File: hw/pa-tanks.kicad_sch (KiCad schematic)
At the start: 62 parts, among them K2202 G2RL-1A, K2203 G2RL-1A, K2204 G2RL-1A, Q2201 2N7002, Q2202 2N7002, Q2203 2N7002, Q2204 2N7002, Q2205 2N7002, Q2206 2N7002, Q2207 2N7002, Q2208 2N7002, Q2209 2N7002, Q2210 2N7002

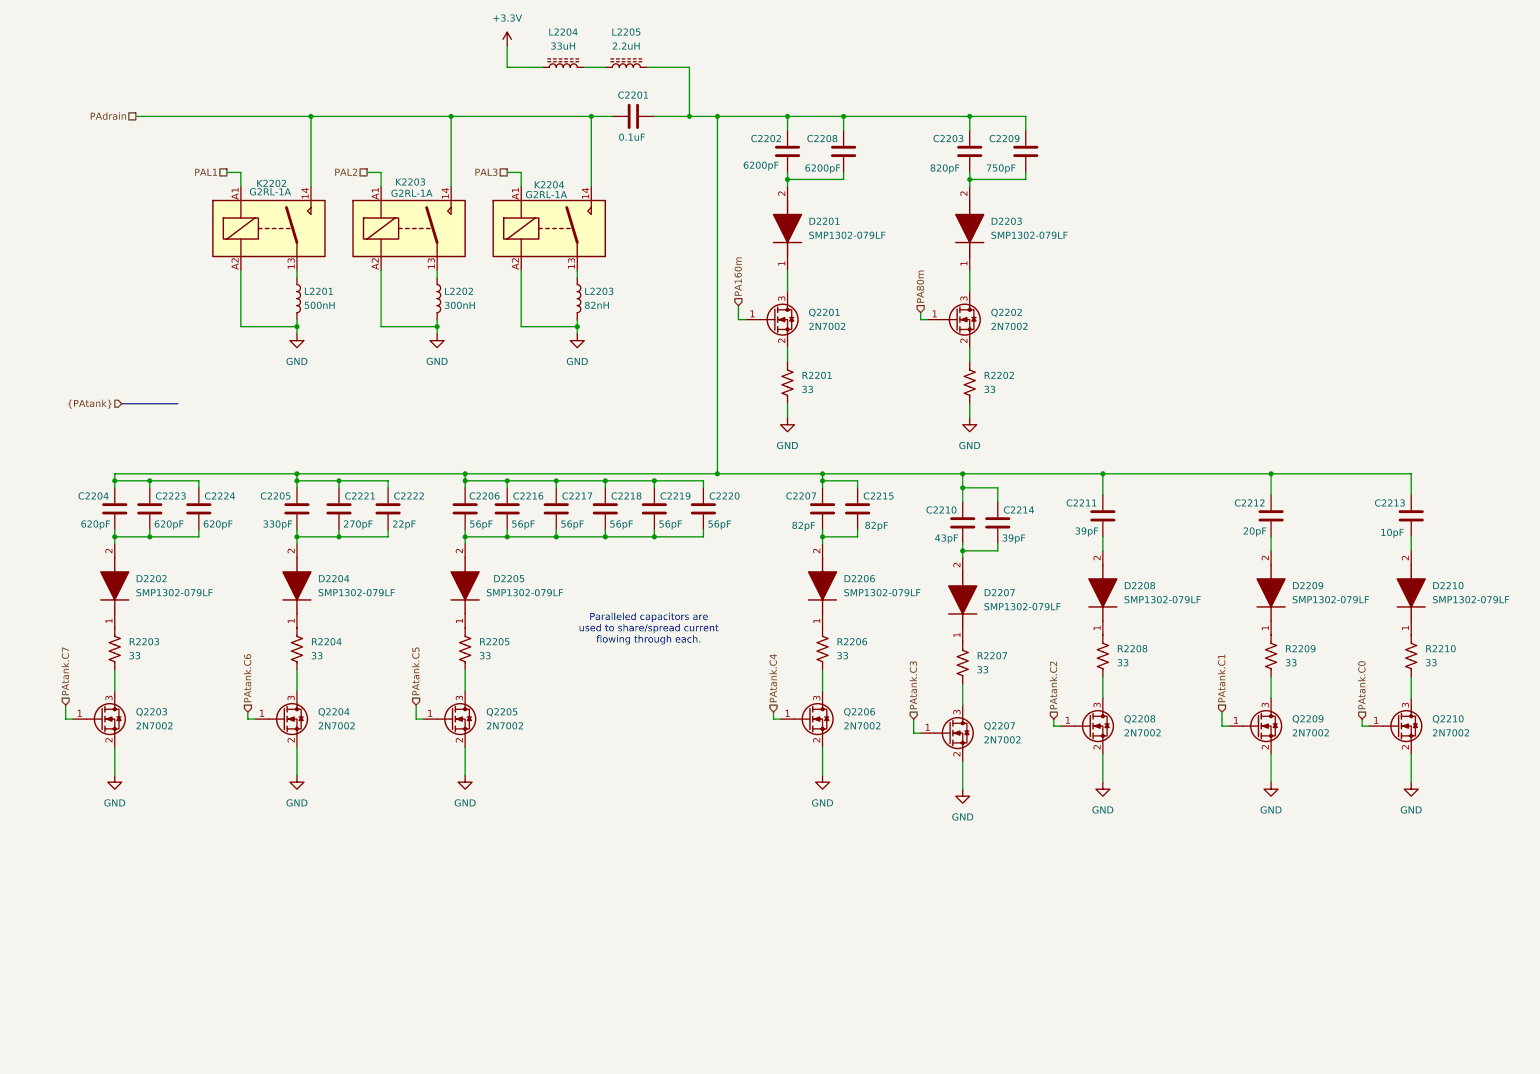
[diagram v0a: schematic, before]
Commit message: Getting closer to having the PA LC tank switching done
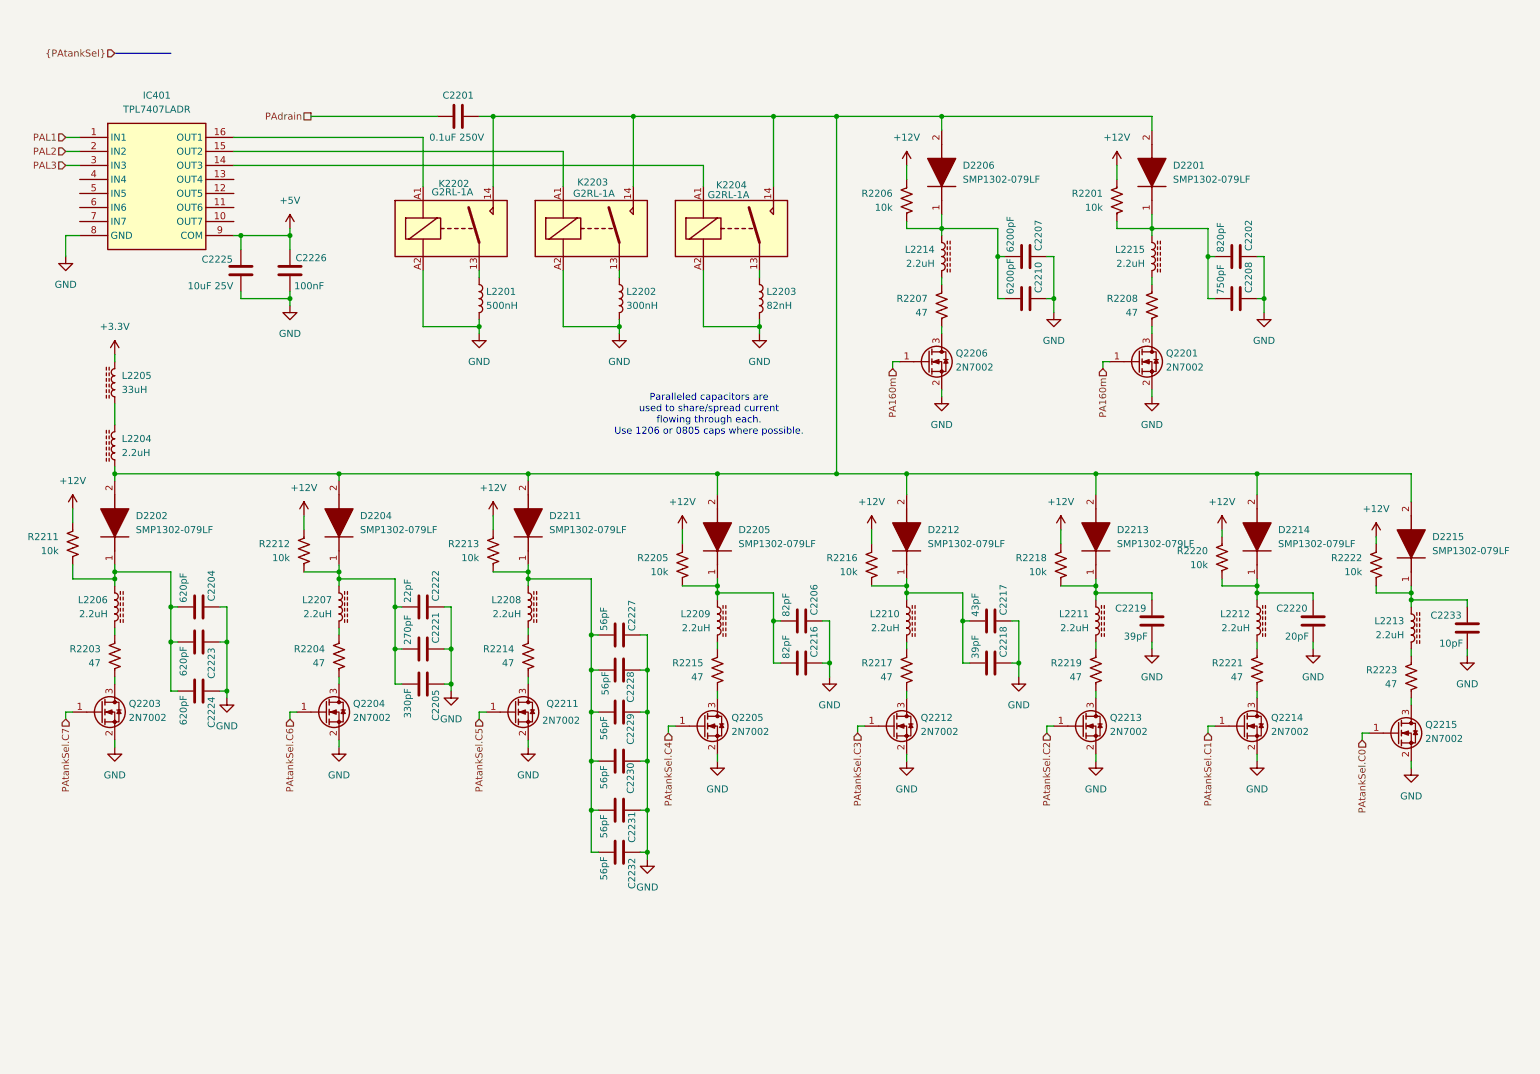
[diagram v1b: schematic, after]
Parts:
- removed C2203: 820pF, symbol Device:C
- removed C2209: 750pF, symbol Device:C
- removed C2211, C2214: 39pF, symbol Device:C
- removed C2212: 20pF, symbol Device:C
- removed C2213: 10pF, symbol Device:C
- removed C2215: 82pF, symbol Device:C
- removed D2203, D2207, D2208, D2209, D2210: SMP1302-079LF, SODFL1608X70N, symbol SMP1302-079LF:SMP1302-079LF
- removed Q2202, Q2207, Q2208, Q2209, Q2210: 2N7002, Package_TO_SOT_SMD:SOT-23, symbol Transistor_FET:2N7002
- removed R2202, R2209, R2210: 33, symbol Device:R_US
- added C2225: 10uF 25V, symbol Device:C
- added C2226: 100nF, symbol Device:C
- added C2227, C2228, C2229, C2230, C2231, C2232: 56pF, symbol Device:C
- added C2233: 10pF, symbol Device:C
- added D2211, D2212, D2213, D2214, D2215: SMP1302-079LF, SODFL1608X70N, symbol SMP1302-079LF:SMP1302-079LF
- added IC401: TPL7407LADR, SOIC127P600X175-16N, symbol TPL7407LADR:TPL7407LADR
- added L2206, L2207, L2208, L2209, L2210, L2211, L2212, L2213, L2214, L2215: 2.2uH, symbol Device:L_Ferrite
- added Q2211, Q2212, Q2213, Q2214, Q2215: 2N7002, Package_TO_SOT_SMD:SOT-23, symbol Transistor_FET:2N7002
- added R2211, R2212, R2213, R2216, R2218, R2220, R2222: 10k, symbol Device:R_US
- added R2214, R2215, R2217, R2219, R2221, R2223: 47, symbol Device:R_US
- C2201: value 0.1uF -> 0.1uF 250V
- C2202: value 6200pF -> 820pF
- C2206, C2216: value 56pF -> 82pF
- C2207: value 82pF -> 6200pF
- C2208: value 6200pF -> 750pF
- C2210: value 43pF -> 6200pF
- C2217: value 56pF -> 43pF
- C2218, C2219: value 56pF -> 39pF
- C2220: value 56pF -> 20pF
- L2204: value 33uH -> 2.2uH
- L2205: value 2.2uH -> 33uH
- R2201, R2205, R2206: value 33 -> 10k
- R2203, R2204, R2207, R2208: value 33 -> 47
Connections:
- net PAtank.C4 is gone; now on net PA160m: Q2206.1 (G)
- net +3.3V: now also L2205.2; no longer L2204.1
- net GND: now also C2202.2, C2204.2, C2205.2, C2206.2, C2207.2, C2208.2, C2210.2, C2216.2, C2217.2, C2218.2, C2219.1, C2220.1, C2221.2, C2222.2, C2223.2, C2224.2, Q2201.2 (S), C2225.1, C2226.1, C2227.2, C2228.2, C2229.2, C2230.2, C2231.2, C2232.2, C2233.1, IC401.8 (GND), Q2211.2 (S), Q2212.2 (S), Q2213.2 (S), Q2214.2 (S), Q2215.2 (S); no longer R2201.2
- net PAL1: now also IC401.1 (IN1); no longer K2202.A1
- net PAL2: now also IC401.2 (IN2); no longer K2203.A1
- net PAL3: now also IC401.3 (IN3); no longer K2204.A1
- net PAdrain: no longer K2202.14, K2203.14, K2204.14
- net at D2205.1 (K): now also C2206.1, C2216.1, R2205.2, L2209.2; no longer R2205.1
- net at R2208.2: now also Q2201.3 (D)
- net at D2206.2 (A): now also C2201.2, D2201.2 (A), D2202.2 (A), D2204.2 (A), D2205.2 (A), K2202.14, K2203.14, K2204.14, L2204.1, D2211.2 (A), D2212.2 (A), D2213.2 (A), D2214.2 (A), D2215.2 (A); no longer C2207.1
- net at C2210.1: now also C2207.1, D2206.1 (K), R2206.2, L2214.2
- net at Q2205.3 (D): now also R2215.2; no longer R2205.2
- net at C2204.1, C2223.1, C2224.1: now also D2202.1 (K), L2206.2, R2211.2; no longer D2202.2 (A)
- net at C2202.1, C2208.1: now also D2201.1 (K), R2201.2, L2215.2; no longer D2201.2 (A)
- net at R2207.1: now also L2214.1
- net +12V: now reaches R2206.1
- net +12V: now also R2201.1, R2205.1, R2211.1, R2212.1, R2213.1, R2216.1, R2218.1, R2220.1, R2222.1; no longer D2206.1 (K)
- net at Q2206.3 (D): now also R2207.2; no longer R2206.2
- net at R2203.1: now also L2206.1; no longer D2202.1 (K)
- net at C2205.1, C2221.1, C2222.1: now also D2204.1 (K), L2207.2, R2212.2; no longer D2204.2 (A)
- net at R2204.1: now also L2207.1; no longer D2204.1 (K)
- net at R2208.1: now also L2215.1
- net PAtank.C5 renamed PAtankSel.C4
- net PAtank.C6 renamed PAtankSel.C6
- net PAtank.C7 renamed PAtankSel.C7
- new net: L2212.1, R2221.1
- new net: Q2214.3 (D), R2221.2
- new net: C2220.2, D2214.1 (K), L2212.2, R2220.2
- new net: IC401.16 (OUT1), K2202.A1
- new net: C2227.1, C2228.1, C2229.1, C2230.1, C2231.1, C2232.1, D2211.1 (K), L2208.2, R2213.2
- new net: Q2212.3 (D), R2217.2
- new net: L2209.1, R2215.1
- new net: Q2215.3 (D), R2223.2
- new net: C2219.2, D2213.1 (K), L2211.2, R2218.2
- new net: L2210.1, R2217.1
- new net: C2217.1, C2218.1, D2212.1 (K), L2210.2, R2216.2
- new net: L2211.1, R2219.1
- new net: L2208.1, R2214.1
- new net: Q2211.3 (D), R2214.2
- new net: IC401.14 (OUT3), K2204.A1
- new net: C2233.2, D2215.1 (K), L2213.2, R2222.2
- new net: IC401.15 (OUT2), K2203.A1
- new net: Q2213.3 (D), R2219.2
- new net: L2213.1, R2223.1
- new net +5V: C2225.2, C2226.2, IC401.9 (COM)
- new net PAtankSel.C0: Q2215.1 (G)
- new net PAtankSel.C1: Q2214.1 (G)
- new net PAtankSel.C2: Q2213.1 (G)
- new net PAtankSel.C3: Q2212.1 (G)
- new net PAtankSel.C5: Q2211.1 (G)
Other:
- note added: "Paralleled capacitors are used to share/spread current flowing through each. Use 1206 or 0805 caps where possible."
- note removed: "Paralleled capacitors are used to share/spread current flowing through each."
- moved on the sheet: C2201, C2204, C2205, C2221, C2222, C2223, C2224, D2202, D2204, K2202, K2203, K2204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

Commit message: Tx LPF and its selection is pretty much done. Fix some OCD. Start to describe the design and construction.
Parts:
- renumbered C2204 to C2201, C2223 to C2202, C2224 to C2203, C2225 to C2204, C2226 to C2205, C2222 to C2206, C2221 to C2207, C2205 to C2208, C2201 to C2209, C2227 to C2210, C2228 to C2211, C2229 to C2212, C2230 to C2213, C2231 to C2214, C2232 to C2215, C2206 to C2216, C2216 to C2217, C2217 to C2218, C2218 to C2219, C2207 to C2220, C2210 to C2221, C2219 to C2222, C2202 to C2223, C2208 to C2224, C2220 to C2225, C2233 to C2226, D2202 to D2201, D2204 to D2202, D2211 to D2203, D2205 to D2204, D2212 to D2205, D2213 to D2207, D2201 to D2208, D2214 to D2209, D2215 to D2210, IC401 to IC2201, K2202 to K2201, K2203 to K2202, K2204 to K2203, L2205 to L2201, L2204 to L2202, L2206 to L2203, L2207 to L2204, L2201 to L2205, L2208 to L2206, L2202 to L2207, L2209 to L2208, L2203 to L2209, L2214 to L2211, L2211 to L2212, L2215 to L2213, L2212 to L2214, L2213 to L2215, Q2203 to Q2201, Q2204 to Q2202, Q2211 to Q2203, Q2205 to Q2204, Q2212 to Q2205, Q2213 to Q2207, Q2201 to Q2208, Q2214 to Q2209, Q2215 to Q2210, R2211 to R2201, R2203 to R2202, R2212 to R2203, R2213 to R2205, R2214 to R2206, R2205 to R2207, R2215 to R2208, R2216 to R2209, R2206 to R2210, R2217 to R2211, R2207 to R2212, R2218 to R2213, R2219 to R2214, R2201 to R2215, R2208 to R2216, R2220 to R2217, R2221 to R2218, R2222 to R2219, R2223 to R2220
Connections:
- net PA160m: no longer Q2208.1 (G)
- new net PA80m: Q2208.1 (G)

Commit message: Checkpoint
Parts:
- removed C2209: 0.1uF 250V, symbol Device:C
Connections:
- net PAdrain: now also D2201.2 (A), D2202.2 (A), D2203.2 (A), D2204.2 (A), D2205.2 (A), D2206.2 (A), D2207.2 (A), D2208.2 (A), D2209.2 (A), D2210.2 (A), K2201.14, K2202.14, K2203.14, L2202.1
- net PAtankSel.C0: no longer Q2210.1 (G)
- net PAtankSel.C1: no longer Q2209.1 (G)
- net PAtankSel.C2: no longer Q2207.1 (G)
- net PAtankSel.C3: no longer Q2205.1 (G)
- net PAtankSel.C4: no longer Q2204.1 (G)
- net PAtankSel.C5: no longer Q2203.1 (G)
- net PAtankSel.C6: no longer Q2202.1 (G)
- net PAtankSel.C7: no longer Q2201.1 (G)
- net TxRelay: now reaches IC2201.10 (OUT7)
- net TxEnable: now reaches IC2201.7 (IN7)
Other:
- moved on the sheet: C2204, C2205, IC2201

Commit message: Veer buck/boost schematic now seems done.
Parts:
- renumbered C2210 to C2209, C2211 to C2210, C2212 to C2211, C2213 to C2212, C2214 to C2213, C2215 to C2214, C2216 to C2215, C2217 to C2216, C2218 to C2217, C2219 to C2218, C2220 to C2219, C2221 to C2220, C2222 to C2221, C2223 to C2222, C2224 to C2223, C2225 to C2224, C2226 to C2225
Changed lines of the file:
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@@
 		(on_board yes)
 		(dnp no)
-		(property "Reference" "C2224"
+		(property "Reference" "C2223"
 			(at 234.696 66.294 0)
 			(effects
@@
 			(project "USB-SSB-txcvr"
 				(path "/8ae46c04-d01a-4756-8774-512b694bfaff/2406d03c-531b-4eaf-8b4b-4b266b9d0f2b/0f153e91-311c-48a1-9871-c6d6a5339cb3"
-					(reference "C2224")
+					(reference "C2223")
 					(unit 1)
 				)
@@
 		(dnp no)
 		(fields_autoplaced yes)
-		(property "Reference" "#PWR02202"
+		(property "Reference" "#PWR02201"
 			(at 21.59 109.22 0)
 			(effects
@@
 			(project "USB-SSB-txcvr"
 				(path "/8ae46c04-d01a-4756-8774-512b694bfaff/2406d03c-531b-4eaf-8b4b-4b266b9d0f2b/0f153e91-311c-48a1-9871-c6d6a5339cb3"
-					(reference "#PWR02202")
+					(reference "#PWR02201")
 					(unit 1)
 				)
@@
 		(on_board yes)
 		(dnp no)
-		(property "Reference" "C2215"
+		(property "Reference" "C2214"
 			(at 122.936 168.656 0)
 			(effects
@@
 			(project "USB-SSB-txcvr"
 				(path "/8ae46c04-d01a-4756-8774-512b694bfaff/2406d03c-531b-4eaf-8b4b-4b266b9d0f2b/0f153e91-311c-48a1-9871-c6d6a5339cb3"
-					(reference "C2215")
+					(reference "C2214")
 					(unit 1)
 				)
@@
 		(on_board yes)
 		(dnp no)
-		(property "Reference" "C2212"
+		(property "Reference" "C2211"
 			(at 122.682 142.494 0)
 			(effects
@@
 			(project "USB-SSB-txcvr"
 				(path "/8ae46c04-d01a-4756-8774-512b694bfaff/2406d03c-531b-4eaf-8b4b-4b266b9d0f2b/0f153e91-311c-48a1-9871-c6d6a5339cb3"
-					(reference "C2212")
+					(reference "C2211")
 					(unit 1)
 				)
@@
 		(on_board yes)
 		(dnp no)
-		(property "Reference" "C2217"
+		(property "Reference" "C2216"
 			(at 155.956 132.334 0)
 			(effects
@@
 			(project "USB-SSB-txcvr"
 				(path "/8ae46c04-d01a-4756-8774-512b694bfaff/2406d03c-531b-4eaf-8b4b-4b266b9d0f2b/0f153e91-311c-48a1-9871-c6d6a5339cb3"
-					(reference "C2217")
+					(reference "C2216")
 					(unit 1)
 				)
@@
 		(on_board yes)
 		(dnp no)
-		(property "Reference" "C2226"
+		(property "Reference" "C2225"
 			(at 273.304 124.714 0)
 			(effects
@@
 			(project "USB-SSB-txcvr"
 				(path "/8ae46c04-d01a-4756-8774-512b694bfaff/2406d03c-531b-4eaf-8b4b-4b266b9d0f2b/0f153e91-311c-48a1-9871-c6d6a5339cb3"
-					(reference "C2226")
+					(reference "C2225")
 					(unit 1)
 				)
@@
 		(on_board yes)
 		(dnp no)
-		(property "Reference" "C2220"
+		(property "Reference" "C2219"
 			(at 196.596 58.674 0)
 			(effects
@@
 			(project "USB-SSB-txcvr"
 				(path "/8ae46c04-d01a-4756-8774-512b694bfaff/2406d03c-531b-4eaf-8b4b-4b266b9d0f2b/0f153e91-311c-48a1-9871-c6d6a5339cb3"
-					(reference "C2220")
+					(reference "C2219")
 					(unit 1)
 				)
@@
 		(on_board yes)
 		(dnp no)
-		(property "Reference" "C2216"
+		(property "Reference" "C2215"
 			(at 155.956 124.714 0)
 			(effects
@@
 			(project "USB-SSB-txcvr"
 				(path "/8ae46c04-d01a-4756-8774-512b694bfaff/2406d03c-531b-4eaf-8b4b-4b266b9d0f2b/0f153e91-311c-48a1-9871-c6d6a5339cb3"
-					(reference "C2216")
+					(reference "C2215")
 					(unit 1)
 				)
@@
 		(on_board yes)
 		(dnp no)
-		(property "Reference" "C2219"
+		(property "Reference" "C2218"
 			(at 190.246 132.334 0)
 			(effects
@@
 			(project "USB-SSB-txcvr"
 				(path "/8ae46c04-d01a-4756-8774-512b694bfaff/2406d03c-531b-4eaf-8b4b-4b266b9d0f2b/0f153e91-311c-48a1-9871-c6d6a5339cb3"
-					(reference "C2219")
+					(reference "C2218")
 					(unit 1)
 				)
@@
 		(dnp no)
 		(fields_autoplaced yes)
-		(property "Reference" "#PWR02206"
+		(property "Reference" "#PWR02207"
 			(at 69.85 58.42 0)
 			(effects
@@
 			(project ""
 				(path "/8ae46c04-d01a-4756-8774-512b694bfaff/2406d03c-531b-4eaf-8b4b-4b266b9d0f2b/0f153e91-311c-48a1-9871-c6d6a5339cb3"
-					(reference "#PWR02206")
+					(reference "#PWR02207")
 					(unit 1)
 				)
@@
 		(on_board yes)
 		(dnp no)
-		(property "Reference" "C2210"
+		(property "Reference" "C2209"
 			(at 122.936 121.92 0)
 			(effects
@@
 			(project "USB-SSB-txcvr"
 				(path "/8ae46c04-d01a-4756-8774-512b694bfaff/2406d03c-531b-4eaf-8b4b-4b266b9d0f2b/0f153e91-311c-48a1-9871-c6d6a5339cb3"
-					(reference "C2210")
+					(reference "C2209")
 					(unit 1)
 				)
@@
 		(on_board yes)
 		(dnp no)
-		(property "Reference" "C2213"
+		(property "Reference" "C2212"
 			(at 122.682 151.384 0)
 			(effects
@@
 			(project "USB-SSB-txcvr"
 				(path "/8ae46c04-d01a-4756-8774-512b694bfaff/2406d03c-531b-4eaf-8b4b-4b266b9d0f2b/0f153e91-311c-48a1-9871-c6d6a5339cb3"
-					(reference "C2213")
+					(reference "C2212")
 					(unit 1)
 				)
@@
 		(dnp no)
 		(fields_autoplaced yes)
-		(property "Reference" "#PWR02201"
+		(property "Reference" "#PWR02202"
 			(at 24.13 66.04 0)
 			(effects
@@
 			(project "USB-SSB-txcvr"
 				(path "/8ae46c04-d01a-4756-8774-512b694bfaff/2406d03c-531b-4eaf-8b4b-4b266b9d0f2b/0f153e91-311c-48a1-9871-c6d6a5339cb3"
-					(reference "#PWR02201")
+					(reference "#PWR02202")
 					(unit 1)
 				)
@@
 		(on_board yes)
 		(dnp no)
-		(property "Reference" "C2214"
+		(property "Reference" "C2213"
 			(at 122.936 160.274 0)
 			(effects
@@
 			(project "USB-SSB-txcvr"
 				(path "/8ae46c04-d01a-4756-8774-512b694bfaff/2406d03c-531b-4eaf-8b4b-4b266b9d0f2b/0f153e91-311c-48a1-9871-c6d6a5339cb3"
-					(reference "C2214")
+					(reference "C2213")
 					(unit 1)
 				)
@@
 		(on_board yes)
 		(dnp no)
-		(property "Reference" "C2221"
+		(property "Reference" "C2220"
 			(at 196.596 66.294 0)
 			(effects
@@
 			(project "USB-SSB-txcvr"
 				(path "/8ae46c04-d01a-4756-8774-512b694bfaff/2406d03c-531b-4eaf-8b4b-4b266b9d0f2b/0f153e91-311c-48a1-9871-c6d6a5339cb3"
-					(reference "C2221")
+					(reference "C2220")
 					(unit 1)
 				)
@@
 		(on_board yes)
 		(dnp no)
-		(property "Reference" "C2223"
+		(property "Reference" "C2222"
 			(at 234.696 58.674 0)
 			(effects
@@
 			(project "USB-SSB-txcvr"
 				(path "/8ae46c04-d01a-4756-8774-512b694bfaff/2406d03c-531b-4eaf-8b4b-4b266b9d0f2b/0f153e91-311c-48a1-9871-c6d6a5339cb3"
-					(reference "C2223")
+					(reference "C2222")
 					(unit 1)
 				)
@@
 		(on_board yes)
 		(dnp no)
-		(property "Reference" "C2218"
+		(property "Reference" "C2217"
 			(at 190.246 124.714 0)
 			(effects
@@
 			(project "USB-SSB-txcvr"
 				(path "/8ae46c04-d01a-4756-8774-512b694bfaff/2406d03c-531b-4eaf-8b4b-4b266b9d0f2b/0f153e91-311c-48a1-9871-c6d6a5339cb3"
-					(reference "C2218")
+					(reference "C2217")
 					(unit 1)
 				)
@@
 		(dnp no)
 		(fields_autoplaced yes)
-		(property "Reference" "#PWR02207"
+		(property "Reference" "#PWR02208"
 			(at 69.85 74.93 0)
 			(effects
@@
 			(project "USB-SSB-txcvr"
 				(path "/8ae46c04-d01a-4756-8774-512b694bfaff/2406d03c-531b-4eaf-8b4b-4b266b9d0f2b/0f153e91-311c-48a1-9871-c6d6a5339cb3"
-					(reference "#PWR02207")
+					(reference "#PWR02208")
 					(unit 1)
 				)
@@
 		(on_board yes)
 		(dnp no)
-		(property "Reference" "C2211"
+		(property "Reference" "C2210"
 			(at 122.682 134.874 0)
 			(effects
@@
 			(project "USB-SSB-txcvr"
 				(path "/8ae46c04-d01a-4756-8774-512b694bfaff/2406d03c-531b-4eaf-8b4b-4b266b9d0f2b/0f153e91-311c-48a1-9871-c6d6a5339cb3"
-					(reference "C2211")
+					(reference "C2210")
 					(unit 1)
 				)
@@
 		(dnp no)
 		(fields_autoplaced yes)
-		(property "Reference" "#PWR02208"
+		(property "Reference" "#PWR02206"
 			(at 63.5 110.49 0)
 			(effects
@@
 			(project "USB-SSB-txcvr"
 				(path "/8ae46c04-d01a-4756-8774-512b694bfaff/2406d03c-531b-4eaf-8b4b-4b266b9d0f2b/0f153e91-311c-48a1-9871-c6d6a5339cb3"
-					(reference "#PWR02208")
+					(reference "#PWR02206")
 					(unit 1)
 				)
@@
 		(on_board yes)
 		(dnp no)
-		(property "Reference" "C2225"
+		(property "Reference" "C2224"
 			(at 245.364 123.444 0)
 			(effects
@@
 			(project "USB-SSB-txcvr"
 				(path "/8ae46c04-d01a-4756-8774-512b694bfaff/2406d03c-531b-4eaf-8b4b-4b266b9d0f2b/0f153e91-311c-48a1-9871-c6d6a5339cb3"
-					(reference "C2225")
+					(reference "C2224")
 					(unit 1)
 				)
@@
 		(on_board yes)
 		(dnp no)
-		(property "Reference" "C2222"
+		(property "Reference" "C2221"
 			(at 216.154 123.444 0)
 			(effects
@@
 			(project "USB-SSB-txcvr"
 				(path "/8ae46c04-d01a-4756-8774-512b694bfaff/2406d03c-531b-4eaf-8b4b-4b266b9d0f2b/0f153e91-311c-48a1-9871-c6d6a5339cb3"
-					(reference "C2222")
+					(reference "C2221")
 					(unit 1)
 				)
